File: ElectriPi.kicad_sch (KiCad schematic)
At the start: 57 parts, among them IC2 TPS51397ARJER, J1 282837-2, J3 JST XH 01x02, J4 282837-2, J6 Raspberry_Pi_2_3, Q1 SiA471DJ, U1 LM73100, U2 COOLING, U3 TVS0500DRV, U4 LM73100

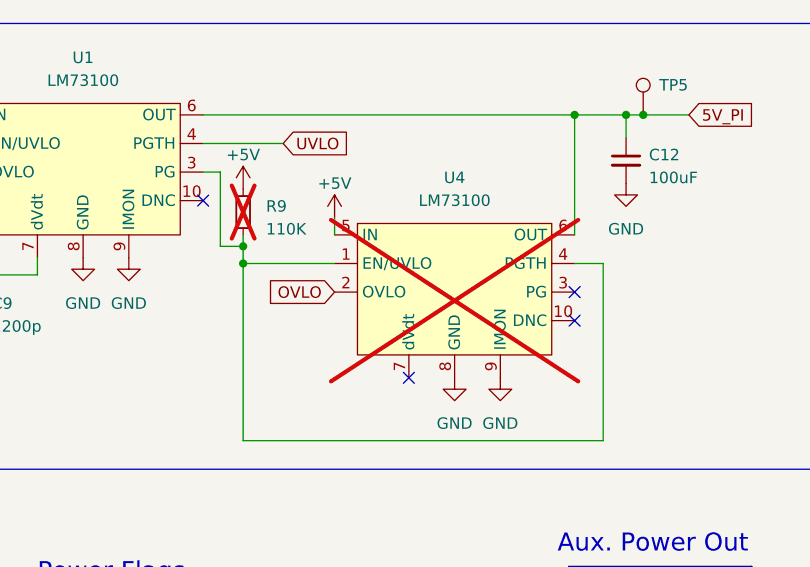
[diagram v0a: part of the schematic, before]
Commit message: Remove DNP on R9 and U4
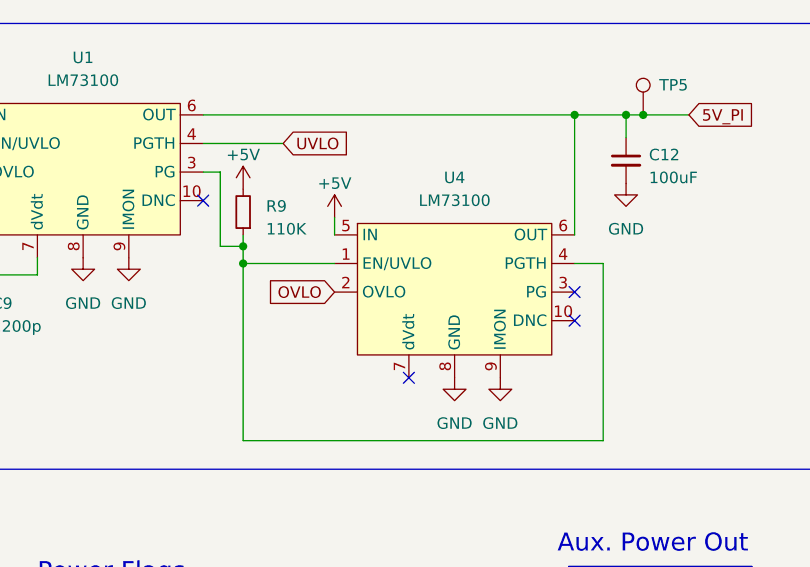
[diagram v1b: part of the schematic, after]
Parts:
- R9, U4: now fitted; now in the parts list
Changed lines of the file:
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@@
   )
   (symbol (lib_id "LM7310:LM73100") (at 139.7 133.35 0) (unit 1)
-    (in_bom no) (on_board yes) (dnp yes) (fields_autoplaced)
+    (in_bom yes) (on_board yes) (dnp no) (fields_autoplaced)
     (property "Reference" "U4" (at 139.7 123.825 0)
       (effects (font (size 1.27 1.27)))
@@
   )
   (symbol (lib_id "Device:R_Small") (at 116.205 127.635 180) (unit 1)
-    (in_bom no) (on_board yes) (dnp yes) (fields_autoplaced)
+    (in_bom yes) (on_board yes) (dnp no) (fields_autoplaced)
     (property "Reference" "R9" (at 118.745 127 0)
       (effects (font (size 1.27 1.27)) (justify right))

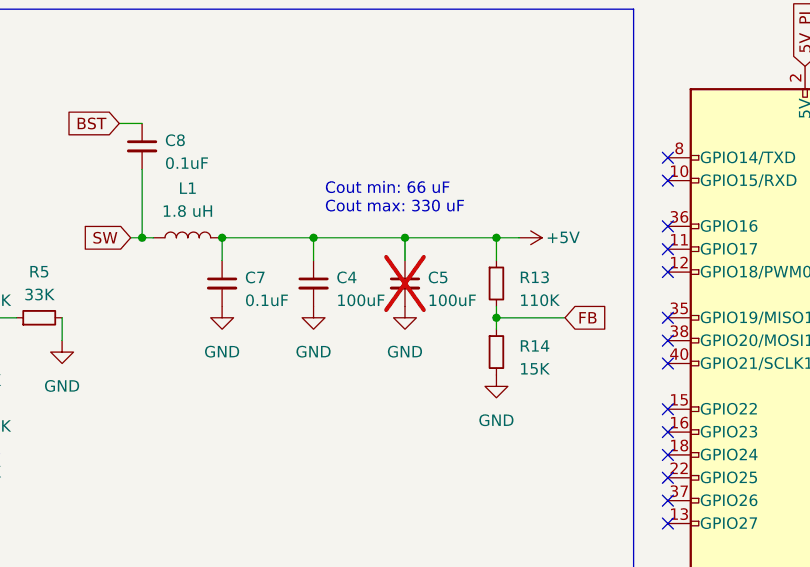
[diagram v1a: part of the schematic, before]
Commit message: revert DNP on C5
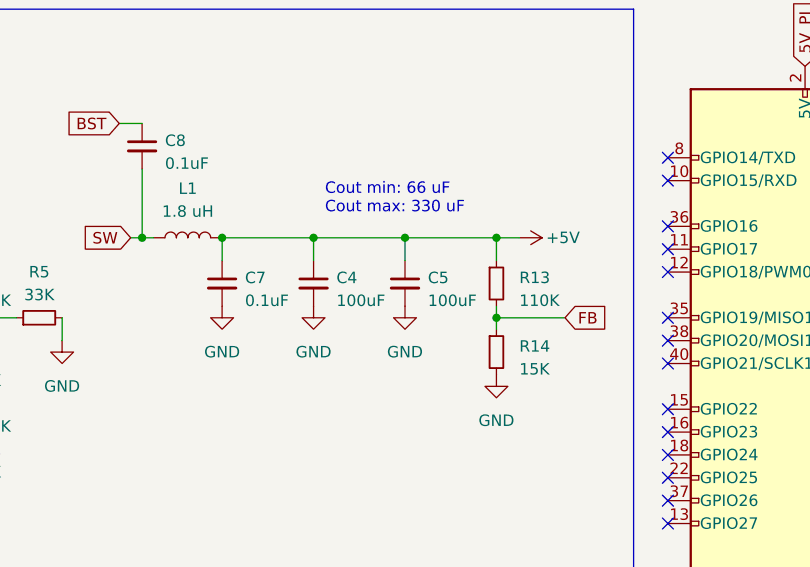
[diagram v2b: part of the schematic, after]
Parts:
- C5: now fitted; now in the parts list
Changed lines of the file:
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@@
   )
   (symbol (lib_id "Device:C_Small") (at 207.01 55.88 0) (unit 1)
-    (in_bom no) (on_board yes) (dnp yes) (fields_autoplaced)
+    (in_bom yes) (on_board yes) (dnp no) (fields_autoplaced)
     (property "Reference" "C5" (at 209.55 55.2513 0)
       (effects (font (size 1.27 1.27)) (justify left))

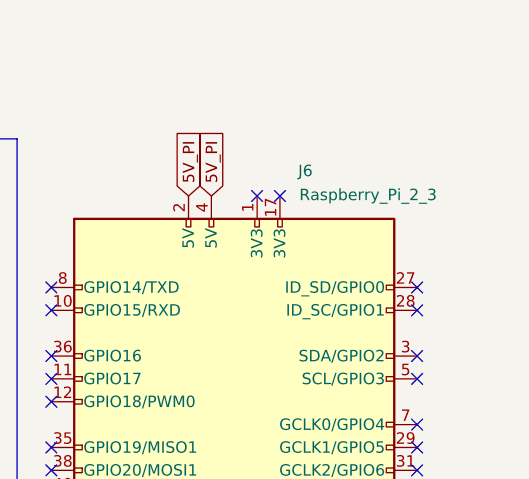
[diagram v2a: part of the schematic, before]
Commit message: Change to 40 pin passthrough header
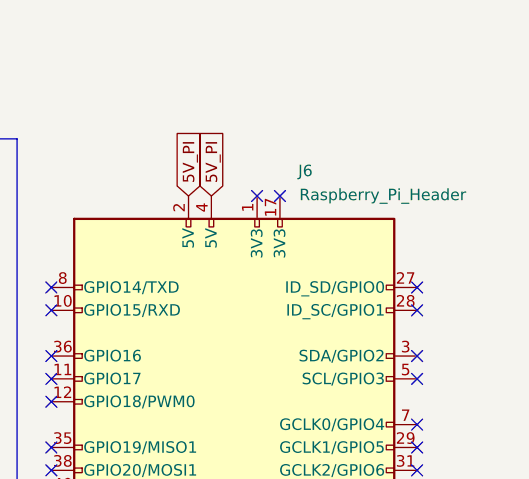
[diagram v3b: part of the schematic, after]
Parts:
- J6: value Raspberry_Pi_2_3 -> Raspberry_Pi_Header; footprint Connector_PinSocket_2.54mm:PinSocket_2x20_P2.54mm_Vertical -> PI_GPIO_PASSTHROUGH:SSM-120-_-DV-BE; DigiKey 1568-PRT-16764-ND -> (none); Mouser 474-PRT-16764 -> (none)

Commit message: V1.1 Updates
Moved status LEDs away from PCB edge.
Moved and modified AUX 5V label.
Changed screw terminals to JST XH.
Added SMD Header LCSC number.
Added 5mm silkscreen for QR Code
Removed silkscreen border for 4010 fan.
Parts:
- J1, J4: value 282837-2 -> JST XH 01x02; footprint TerminalBlock:TerminalBlock_bornier-2_P5.08mm -> Connector_JST:JST_XH_B2B-XH-A_1x02_P2.50mm_Vertical; DigiKey A113320-ND -> (none); LCSC C592976 -> C24193; Mouser 571-2828372 -> (none)
- J6: LCSC (none) -> C22436166
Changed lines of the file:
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@@
 			)
 		)
-		(property "Value" "282837-2"
+		(property "Value" "JST XH 01x02"
 			(at 25.7048 54.61 0)
 			(effects
@@
 			)
 		)
-		(property "Footprint" "TerminalBlock:TerminalBlock_bornier-2_P5.08mm"
+		(property "Footprint" "Connector_JST:JST_XH_B2B-XH-A_1x02_P2.50mm_Vertical"
 			(at 31.75 54.61 0)
 			(effects
@@
 			)
 		)
-		(property "LCSC" "C592976"
+		(property "LCSC" "C24193"
 			(at 31.75 54.61 0)
 			(effects
@@
 			)
 		)
-		(property "DigiKey" "A113320-ND"
+		(property "DigiKey" ""
 			(at 31.75 54.61 0)
 			(effects
@@
 			)
 		)
-		(property "Mouser" "571-2828372"
+		(property "Mouser" ""
 			(at 31.75 54.61 0)
 			(effects
@@
 			)
 		)
-		(property "Value" "282837-2"
+		(property "Value" "JST XH 01x02"
 			(at 166.37 183.2102 0)
 			(effects
@@
 			)
 		)
-		(property "Footprint" "TerminalBlock:TerminalBlock_bornier-2_P5.08mm"
+		(property "Footprint" "Connector_JST:JST_XH_B2B-XH-A_1x02_P2.50mm_Vertical"
 			(at 166.37 177.165 0)
 			(effects
@@
 			)
 		)
-		(property "LCSC" "C592976"
+		(property "LCSC" "C24193"
 			(at 166.37 177.165 0)
 			(effects
@@
 			)
 		)
-		(property "DigiKey" "A113320-ND"
+		(property "DigiKey" ""
 			(at 166.37 177.165 0)
 			(effects
@@
 			)
 		)
-		(property "Mouser" "571-2828372"
+		(property "Mouser" ""
 			(at 166.37 177.165 0)
 			(effects
@@
 			)
 		)
-		(property "LCSC" ""
+		(property "LCSC" "C22436166"
 			(at 256.54 64.77 0)
 			(effects
